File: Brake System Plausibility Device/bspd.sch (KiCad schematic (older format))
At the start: 8 parts

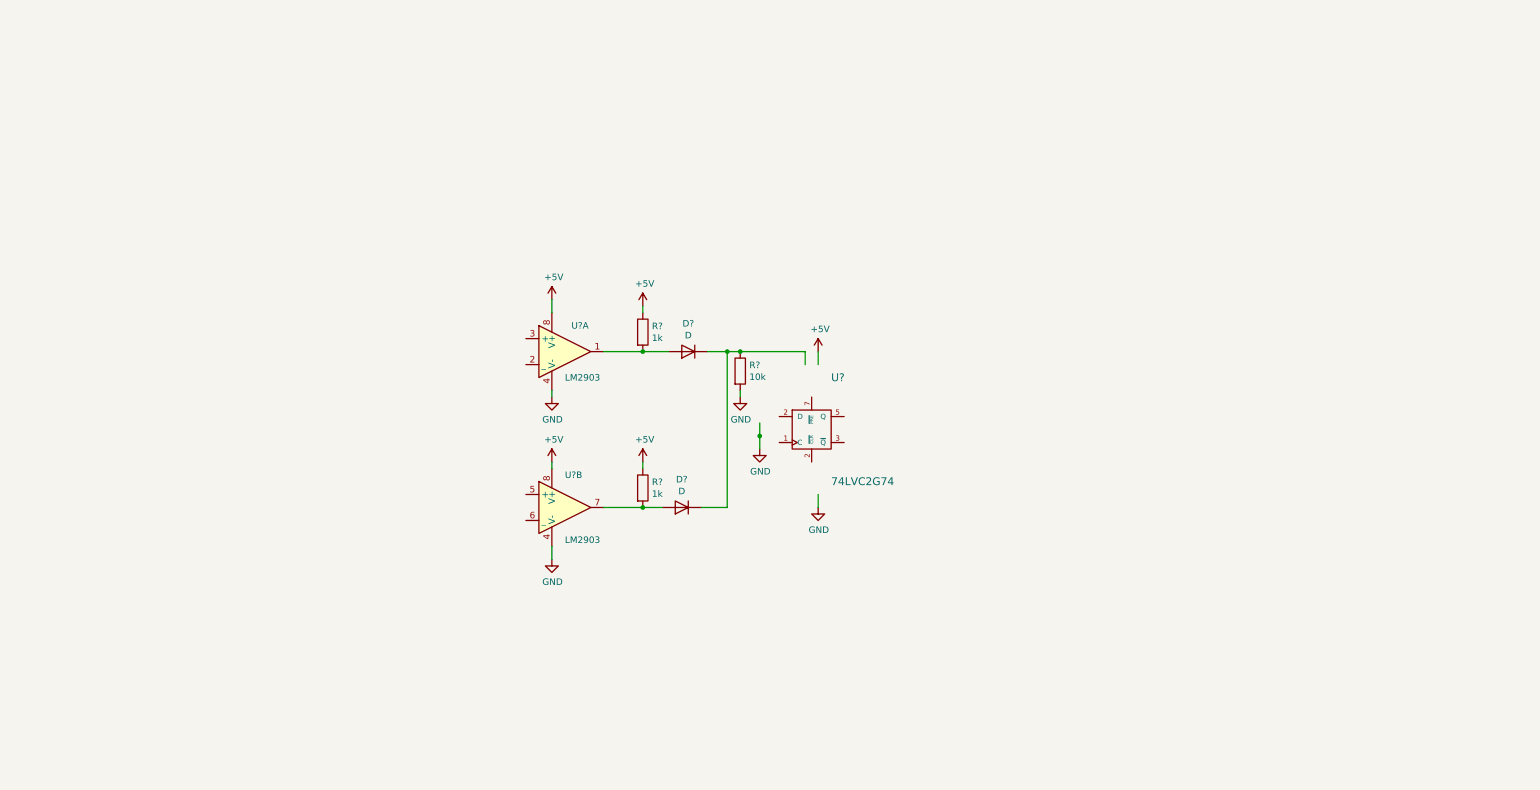
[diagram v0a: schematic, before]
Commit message: BSPD schematic done.
Fuse and power entry included. Needs footprint association and pcb design still. Pausing here so that we have a schematic for the first ESF.
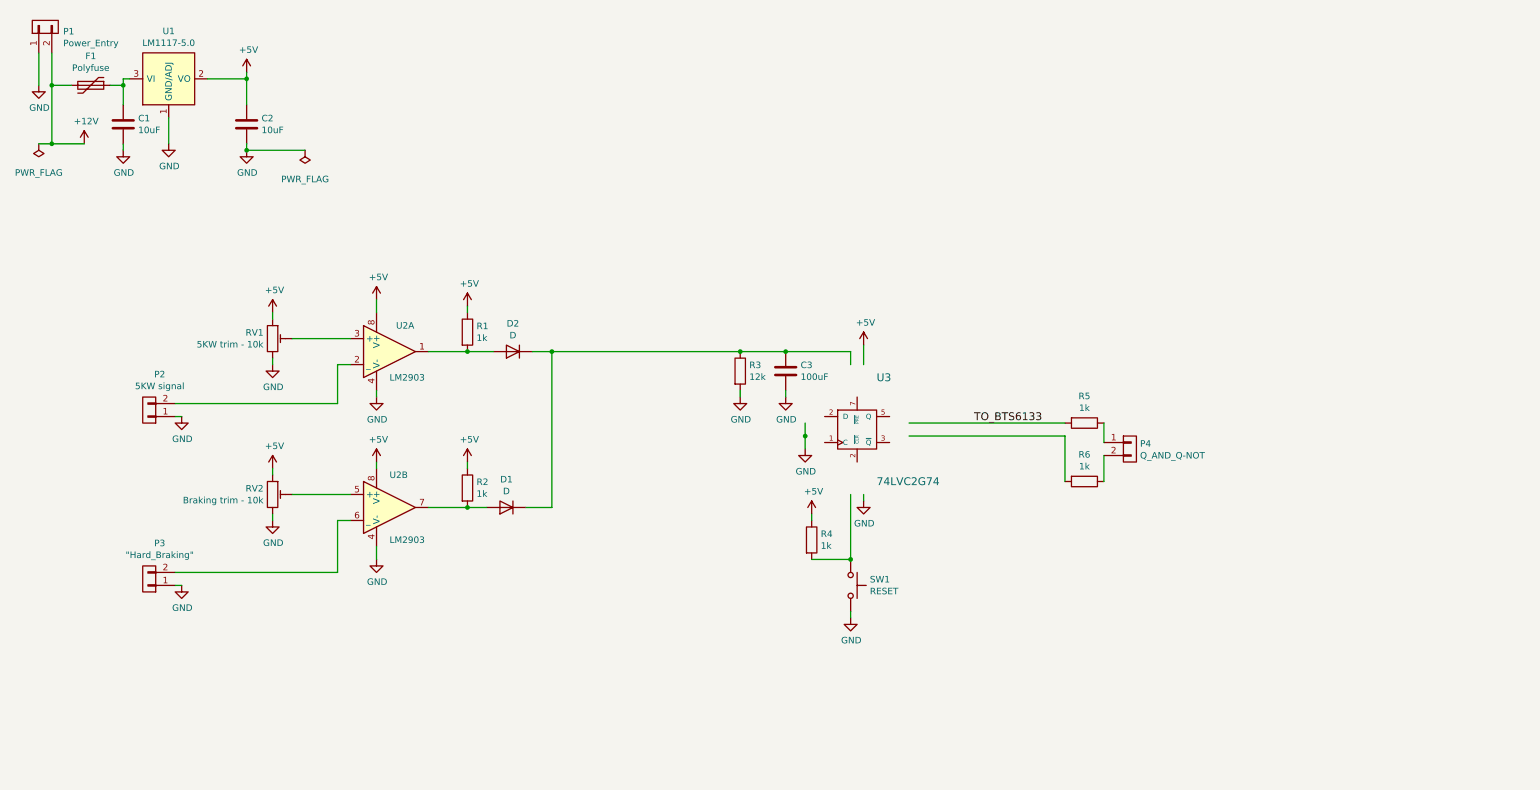
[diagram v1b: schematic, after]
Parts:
- added C1, C2: 10uF, symbol C
- added C3: 100uF, symbol C
- added F1: Polyfuse, symbol Polyfuse
- added P1: Power_Entry, symbol CONN_01X02
- added P2: 5KW signal, symbol CONN_01X02
- added P3: \"Hard_Braking\", symbol CONN_01X02
- added P4: Q_AND_Q-NOT, symbol CONN_01X02
- added R4, R5, R6: 1k, symbol R
- added RV1: 5KW trim - 10k, symbol POT_TRIM
- added RV2: Braking trim - 10k, symbol POT_TRIM
- added SW1: RESET, symbol SW_Push
- added U1: LM1117-5.0, symbol LM1117-5.0
- R3: renamed from R?; value 10k -> 12k
- gave numbers to parts that had none: 6
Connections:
- net labels added: +12V, TO_BTS6133
- wire segments 16 -> 53
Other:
- moved on the sheet: D1, D2, R1, R2, U2A, U2B, U3

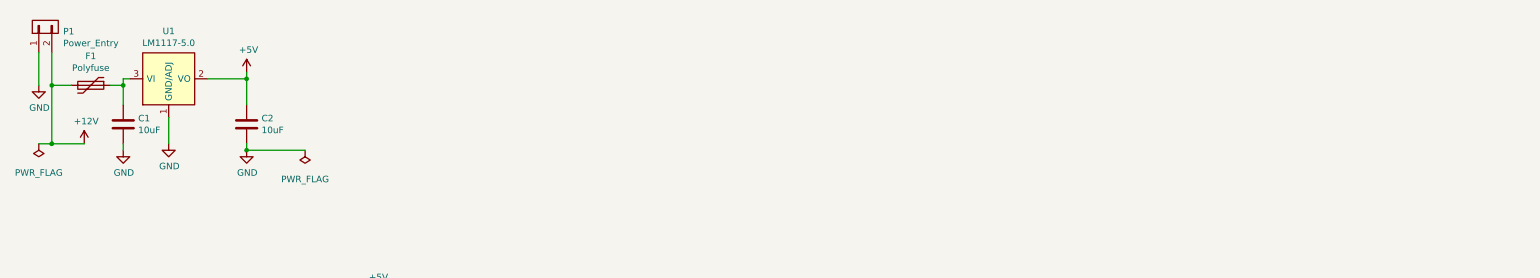
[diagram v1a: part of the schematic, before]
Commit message: BSPD progress, shutdown_circuit
The shutdown_circuit schematic has been started. BSPD component association is half-way done.
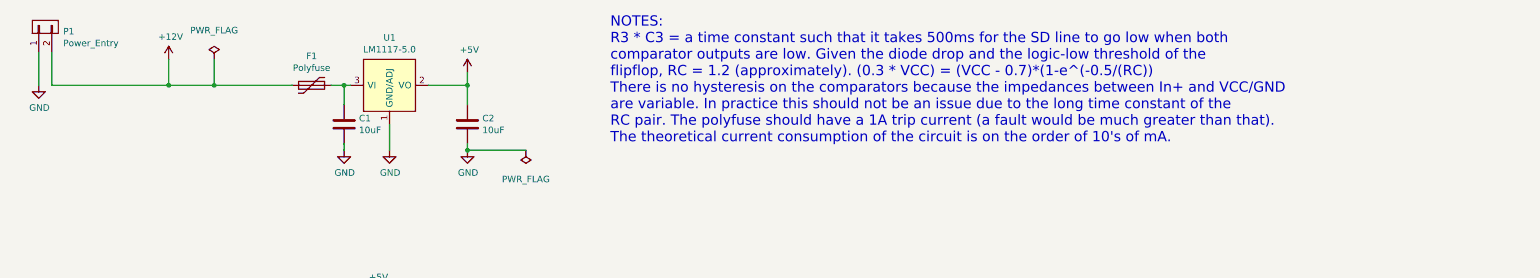
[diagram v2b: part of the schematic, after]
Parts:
- F1: footprint (none) -> SMD_Packages:SMD-1210_Pol
- P1, P2, P3, P4: footprint (none) -> Pin_Headers:Pin_Header_Straight_1x02_Pitch2.54mm
- R1, R2, R3, R4, R5, R6: footprint (none) -> Resistors_SMD:R_0805_HandSoldering
- SW1: footprint (none) -> Wire_Pads:SolderWirePad_2x_1-2mmDrill
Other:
- note added: "NOTES:\nR3 * C3 = a time constant such that it takes 500ms for the SD line to go low when both \ncomparator outputs are low. Given the diode drop and the logic-low threshold of the \nflipflop, RC = 1.2 (approximately). (0.3 * VCC) = (VCC - 0.7)*(1-e^(-0.5/(RC))\nThere is no hysteresis on the comparators because the impedances between In+ and VCC/GND\nare variable. In practice this should not be a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"
- moved on the sheet: C1, C2, F1, U1

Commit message: Fix
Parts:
- removed P2: 5KW signal, Pin_Headers:Pin_Header_Straight_1x02_Pitch2.54mm, symbol CONN_01X02
- added R? (x2): 100k, symbol R
- added U?: TL082, symbol TL082
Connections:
- net labels added: Current_L, Current_R
- wire segments 53 -> 61
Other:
- moved on the sheet: D1, D2, P3, R1, R2, RV1, RV2, U2A, U2B

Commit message: Not sure
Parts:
- gave numbers to parts that had none: 3
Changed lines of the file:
@@
 LIBS:switches
 LIBS:bspd-cache
-EELAYER 26 0
+EELAYER 25 0
 EELAYER END
 $Descr A4 11693 8268
@@
 $EndComp
 $Comp
-L GND #PWR019
+L GND #PWR018
 U 1 1 5875CC6F
 P 3000 4900
-F 0 "#PWR019" H 3000 4650 50  0001 C CNN
+F 0 "#PWR018" H 3000 4650 50  0001 C CNN
 F 1 "GND" H 3005 4727 50  0000 C CNN
 F 2 "" H 3000 4900 50  0000 C CNN
@@
 	4000 950  4000 1200
 $Comp
-L GND #PWR020
+L GND #PWR019
 U 1 1 5875D5B5
 P 4000 1550
-F 0 "#PWR020" H 4000 1300 50  0001 C CNN
+F 0 "#PWR019" H 4000 1300 50  0001 C CNN
 F 1 "GND" H 4005 1377 50  0000 C CNN
 F 2 "" H 4000 1550 50  0000 C CNN
@@
 	4000 1550 4000 1500
 $Comp
-L GND #PWR021
+L GND #PWR020
 U 1 1 5875D639
 P 3400 1550
-F 0 "#PWR021" H 3400 1300 50  0001 C CNN
+F 0 "#PWR020" H 3400 1300 50  0001 C CNN
 F 1 "GND" H 3405 1377 50  0000 C CNN
 F 2 "" H 3400 1550 50  0000 C CNN
@@
 $EndComp
 $Comp
-L GND #PWR022
+L GND #PWR021
 U 1 1 5875D7E4
 P 3050 1550
-F 0 "#PWR022" H 3050 1300 50  0001 C CNN
+F 0 "#PWR021" H 3050 1300 50  0001 C CNN
 F 1 "GND" H 3055 1377 50  0000 C CNN
 F 2 "" H 3050 1550 50  0000 C CNN
@@
 $EndComp
 $Comp
-L PWR_FLAG #FLG023
+L PWR_FLAG #FLG022
 U 1 1 5875D927
 P 4450 1550
-F 0 "#FLG023" H 4450 1645 50  0001 C CNN
+F 0 "#FLG022" H 4450 1645 50  0001 C CNN
 F 1 "PWR_FLAG" H 4450 1773 50  0000 C CNN
 F 2 "" H 4450 1550 50  0000 C CNN
@@
 $EndComp
 $Comp
-L GND #PWR024
+L GND #PWR023
 U 1 1 5875E1BF
 P 700 1050
-F 0 "#PWR024" H 700 800 50  0001 C CNN
+F 0 "#PWR023" H 700 800 50  0001 C CNN
 F 1 "GND" H 705 877 50  0000 C CNN
 F 2 "" H 700 1050 50  0000 C CNN
@@
 	2950 1050 3100 1050
 $Comp
-L PWR_FLAG #FLG025
+L PWR_FLAG #FLG024
 U 1 1 587610F9
 P 2050 850
-F 0 "#FLG025" H 2050 945 50  0001 C CNN
+F 0 "#FLG024" H 2050 945 50  0001 C CNN
 F 1 "PWR_FLAG" H 2050 1073 50  0000 C CNN
 F 2 "" H 2050 850 50  0000 C CNN
@@
 $EndComp
 $Comp
-L +12V #PWR026
+L +12V #PWR025
 U 1 1 58761169
 P 1700 850
-F 0 "#PWR026" H 1700 700 50  0001 C CNN
+F 0 "#PWR025" H 1700 700 50  0001 C CNN
 F 1 "+12V" H 1715 1023 50  0000 C CNN
 F 2 "" H 1700 850 50  0000 C CNN
@@
 $EndComp
 $Comp
-L +5V #PWR027
+L +5V #PWR026
 U 1 1 58761970
 P 4000 950
-F 0 "#PWR027" H 4000 800 50  0001 C CNN
+F 0 "#PWR026" H 4000 800 50  0001 C CNN
 F 1 "+5V" H 4015 1123 50  0000 C CNN
 F 2 "" H 4000 950 50  0000 C CNN
@@
 	5700 3100 6950 3100
 $Comp
-L TL082 U?
+L TL082 U4
 U 1 1 58802F1F
 P 2750 3500
-F 0 "U?" H 2850 3700 50  0000 L CNN
+F 0 "U4" H 2850 3700 50  0000 L CNN
 F 1 "TL082" H 2750 3850 50  0000 L CNN
 F 2 "" H 2750 3500 50  0000 C CNN
@@
 Current_R
 $Comp
-L +5V #PWR?
+L +5V #PWR027
 U 1 1 58803941
 P 2650 3150
-F 0 "#PWR?" H 2650 3000 50  0001 C CNN
+F 0 "#PWR027" H 2650 3000 50  0001 C CNN
 F 1 "+5V" H 2665 3323 50  0000 C CNN
 F 2 "" H 2650 3150 50  0000 C CNN
@@
 	2650 3150 2650 3200
 $Comp
-L GND #PWR?
+L GND #PWR028
 U 1 1 588039EE
 P 2650 3850
-F 0 "#PWR?" H 2650 3600 50  0001 C CNN
+F 0 "#PWR028" H 2650 3600 50  0001 C CNN
 F 1 "GND" H 2655 3677 50  0000 C CNN
 F 2 "" H 2650 3850 50  0000 C CNN
@@
 	2450 4100 3150 4100
 $Comp
-L GND #PWR?
+L GND #PWR029
 U 1 1 58807370
 P 2450 4100
-F 0 "#PWR?" H 2450 3850 50  0001 C CNN
+F 0 "#PWR029" H 2450 3850 50  0001 C CNN
 F 1 "GND" H 2455 3927 50  0000 C CNN
 F 2 "" H 2450 4100 50  0000 C CNN
@@
 $EndComp
 $Comp
-L R R?
+L R R8
 U 1 1 58807782
 P 1700 3600
-F 0 "R?" H 1770 3646 50  0000 L CNN
+F 0 "R8" H 1770 3646 50  0000 L CNN
 F 1 "100k" H 1770 3555 50  0000 L CNN
 F 2 "" V 1630 3600 50  0000 C CNN
@@
 $EndComp
 $Comp
-L R R?
+L R R7
 U 1 1 58807813
 P 1700 3200
-F 0 "R?" H 1770 3246 50  0000 L CNN
+F 0 "R7" H 1770 3246 50  0000 L CNN
 F 1 "100k" H 1770 3155 50  0000 L CNN
 F 2 "" V 1630 3200 50  0000 C CNN

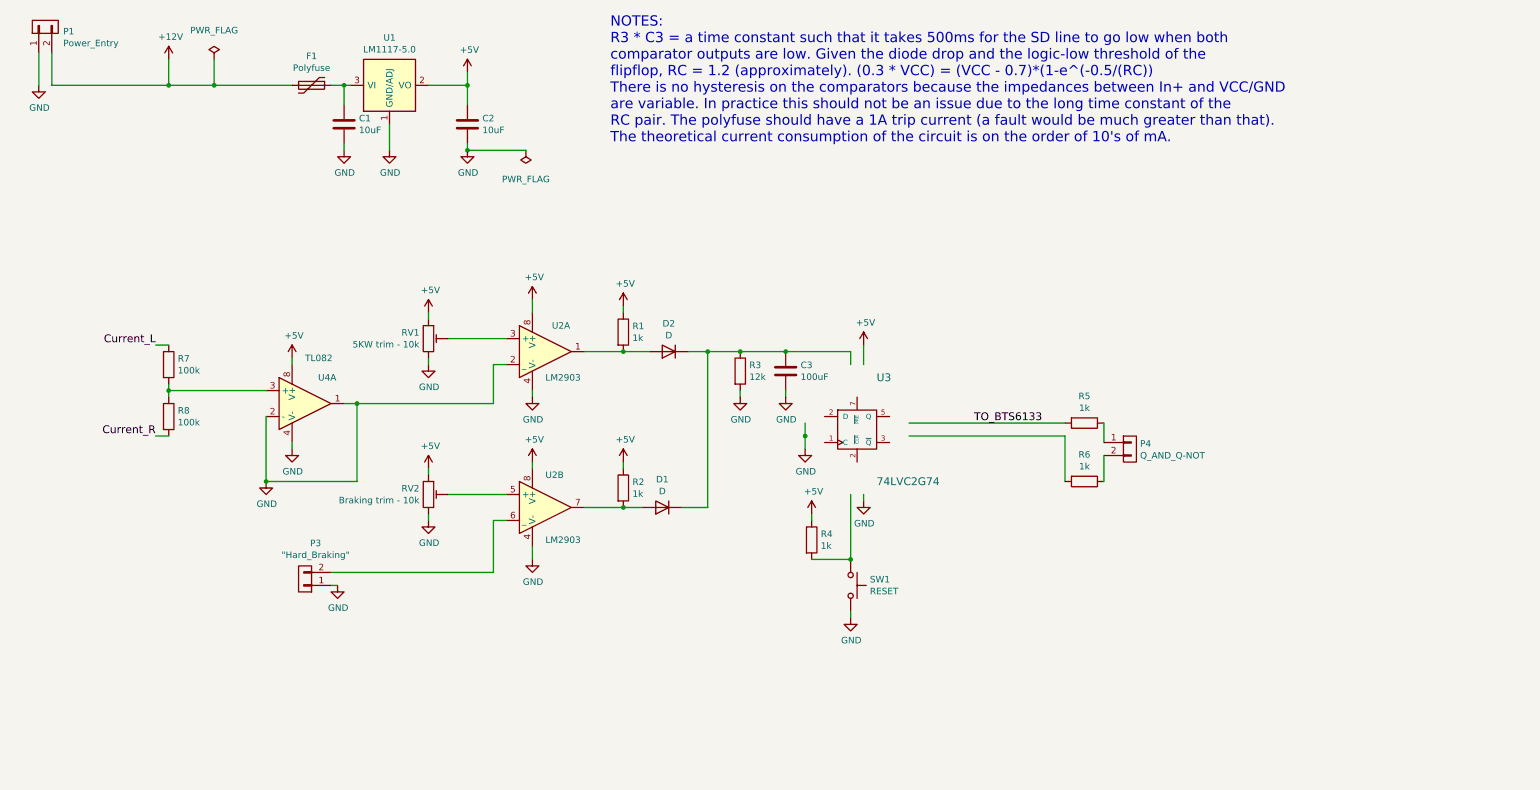
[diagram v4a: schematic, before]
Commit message: BSPD is more fleshed out. IMD latching continuing
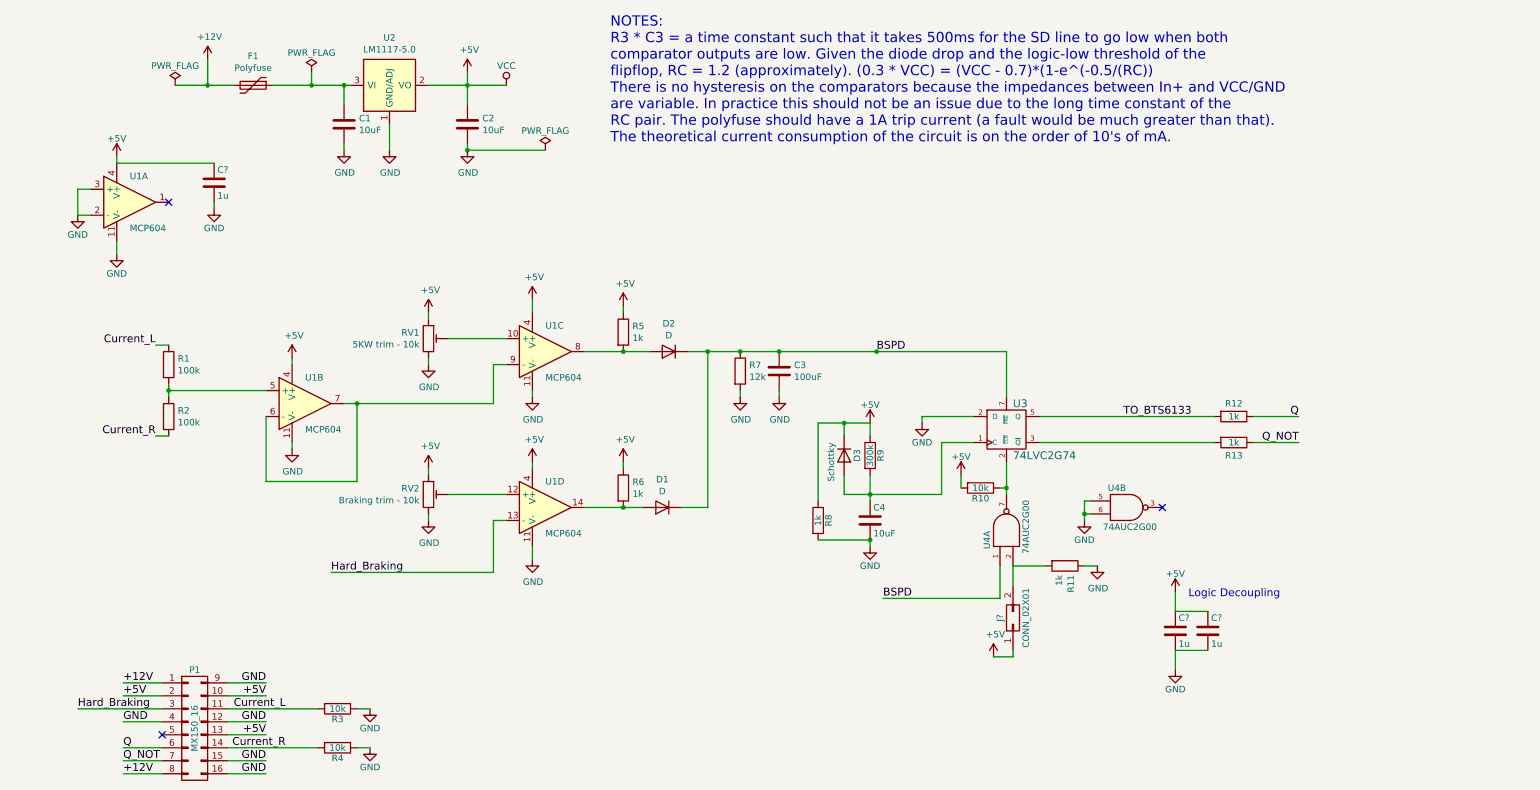
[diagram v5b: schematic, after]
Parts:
- removed P1: Power_Entry, Pin_Headers:Pin_Header_Straight_1x02_Pitch2.54mm, symbol CONN_01X02
- removed P3: \"Hard_Braking\", Pin_Headers:Pin_Header_Straight_1x02_Pitch2.54mm, symbol CONN_01X02
- removed P4: Q_AND_Q-NOT, Pin_Headers:Pin_Header_Straight_1x02_Pitch2.54mm, symbol CONN_01X02
- removed SW1: RESET, Wire_Pads:SolderWirePad_2x_1-2mmDrill, symbol SW_Push
- removed U2: LM2903, symbol LM2903
- removed U4: TL082, symbol TL082
- added C4: 10uF, Capacitors_ThroughHole:CP_Radial_D5.0mm_P2.00mm, symbol C
- added C? (x3): 1u, symbol C
- added D3: Schottky, Diodes_SMD:D_SOD-523, symbol D
- added J?: CONN_02X01, symbol CONN_02X01
- added P1: MX150_16, UNCAMotorsports:MX150_16pin, symbol MX150_16
- added R10, R3, R4: 10k, Resistors_SMD:R_0805_HandSoldering, symbol R
- added R8: 1k, Resistors_SMD:R_0805_HandSoldering, symbol R
- added R9: 300k, Resistors_SMD:R_0805_HandSoldering, symbol R
- added U1: MCP604, Housings_SSOP:TSSOP-14_4.4x5mm_Pitch0.65mm, symbol MCP604
- added U4: 74AUC2G00, Housings_SSOP:VSSOP-8_2.3x2mm_Pitch0.5mm, symbol 74AUC2G00
- C1, C2: footprint (none) -> Capacitors_SMD:C_0805_HandSoldering
- C3: footprint (none) -> Capacitors_ThroughHole:CP_Radial_D5.0mm_P2.00mm
- D1, D2: footprint (none) -> Diodes_SMD:D_MiniMELF_Handsoldering
- R1: renamed from R7; footprint (none) -> Resistors_SMD:R_0805_HandSoldering
- R2: renamed from R8; footprint (none) -> Resistors_SMD:R_0805_HandSoldering
- RV1, RV2: footprint (none) -> Potentiometers:Potentiometer_Trimmer_Bourns_3296W
- U2: renamed from U1; footprint (none) -> TO_SOT_Packages_SMD:SOT-223
- U3: footprint (none) -> Housings_SSOP:TSSOP-8_3x3mm_Pitch0.65mm
- renumbered R4 to R11, R5 to R12, R6 to R13, R1 to R5, R2 to R6, R3 to R7
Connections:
- net labels added: BSPD, Hard_Braking, Q, Q_NOT, VCC
- wire segments 61 -> 104
- no-connect marks 0 -> 3
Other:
- note added: "Logic Decoupling\n"
- moved on the sheet: C3, F1, R11, R12, R13, U3

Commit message: ESF-related changes to current system schematics
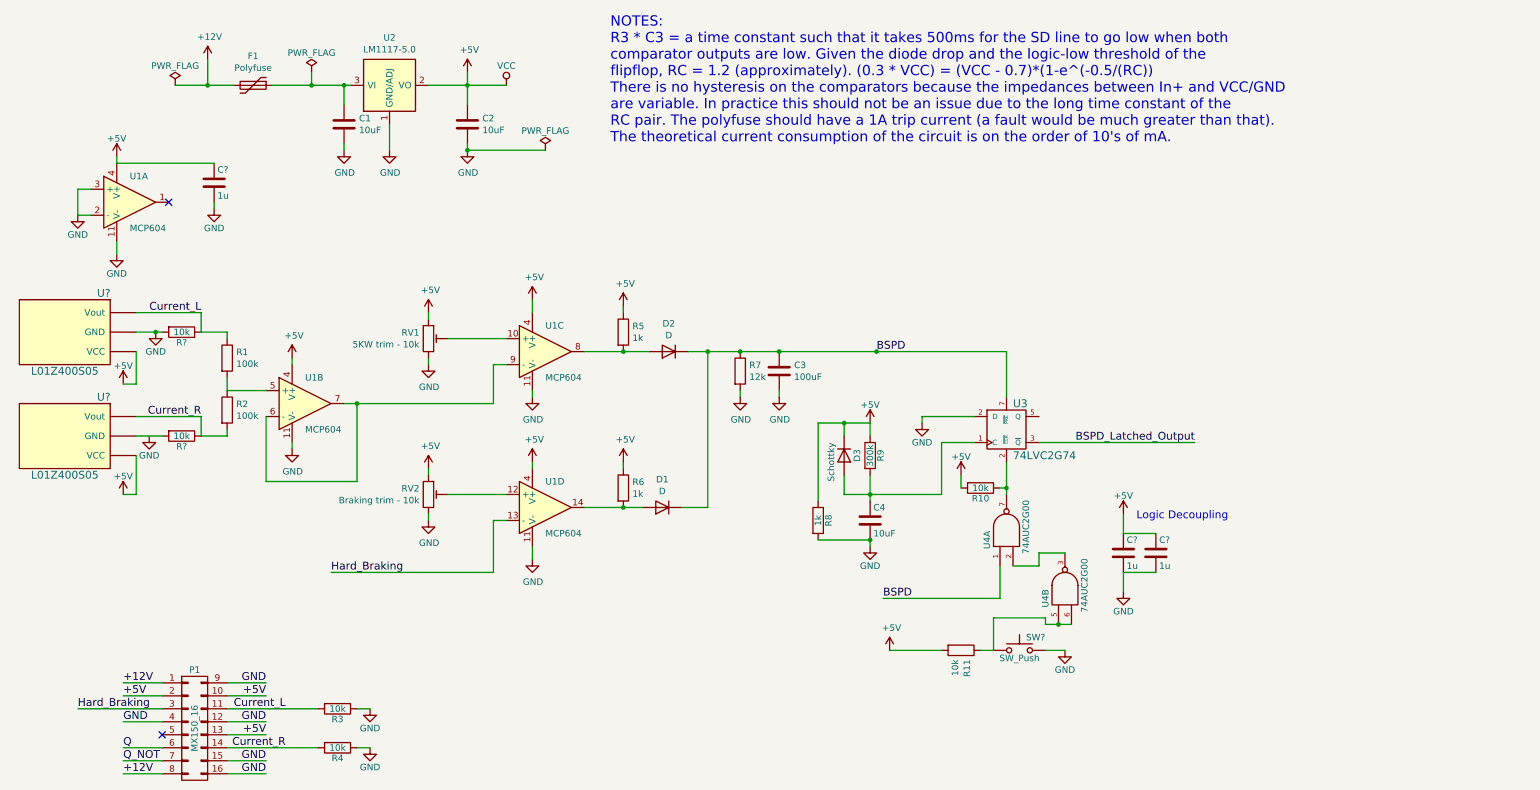
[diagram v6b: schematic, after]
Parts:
- removed J?: CONN_02X01, symbol CONN_02X01
- removed R12, R13: 1k, Resistors_SMD:R_0805_HandSoldering, symbol R
- added R? (x2): 10k, symbol R
- added SW?: SW_Push, symbol SW_Push
- added U? (x2): L01Z400S05, symbol L01Z400S05
- R11: value 1k -> 10k
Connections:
- net +5V: now also R11.2, U?.~ (Vout), U?.~ (Vout)
- net Current_L: now also R?.1, U?.~ (Vout)
- net Current_R: now also R?.1, U?.~ (Vout)
- net GND: now also R?.2, SW?.2, U?.~ (Vout); no longer R11.1, U4.5, U4.6
- net BSPD_Latched_Output: now reaches U3.3 (~Q)
- net at U4.2: now also U4.3; no longer R11.2
- net TO_BTS6133: no longer names the net of U3.5 (Q)
- new net: R11.1, SW?.1, U4.5, U4.6
- new net: R?.2, U?.~ (Vout)
- no-connect marks 3 -> 2
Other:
- moved on the sheet: C?, R1, R11, R2, U4B
